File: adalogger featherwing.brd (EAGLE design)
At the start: 50.8 x 22.9 mm, 22 parts, among them IC1 RTC_PCF8523T, SW1 KMR2, X4 microsd, Y1 32khz

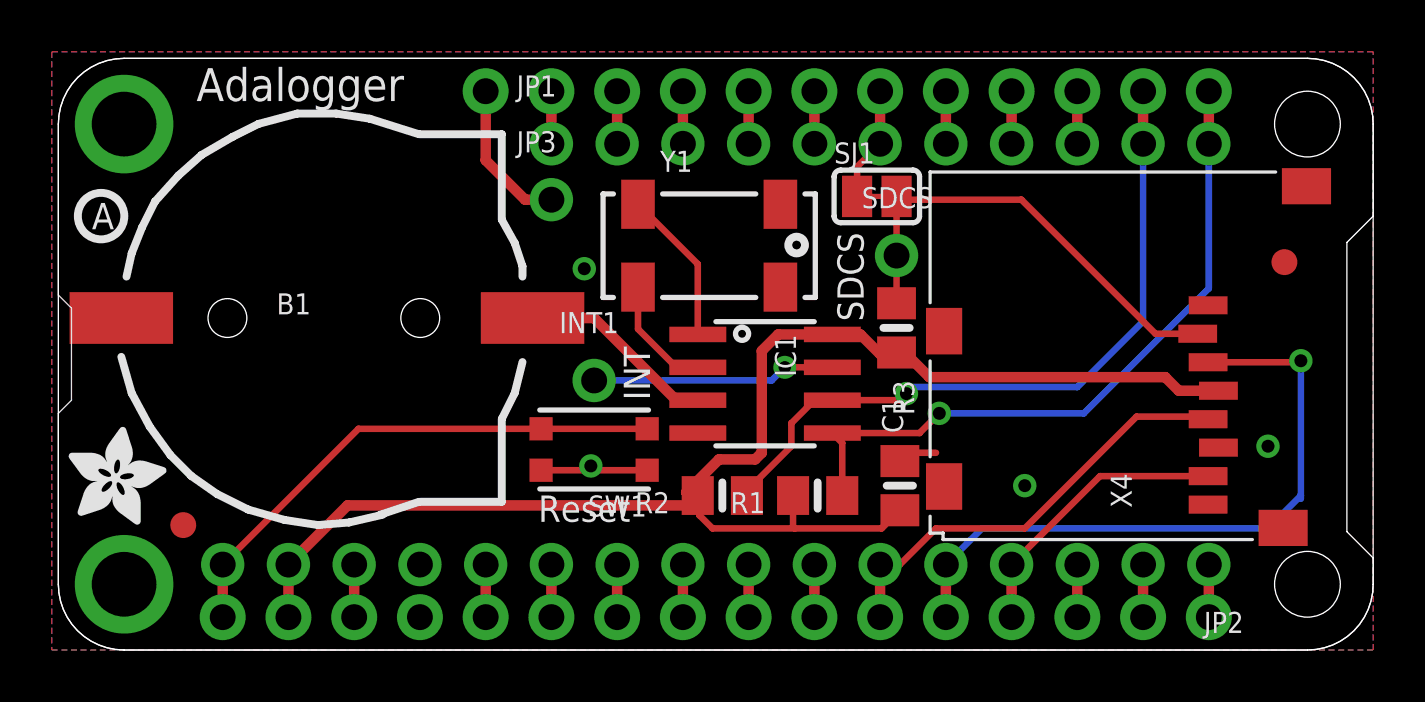
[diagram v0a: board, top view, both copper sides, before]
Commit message: update with RC filter
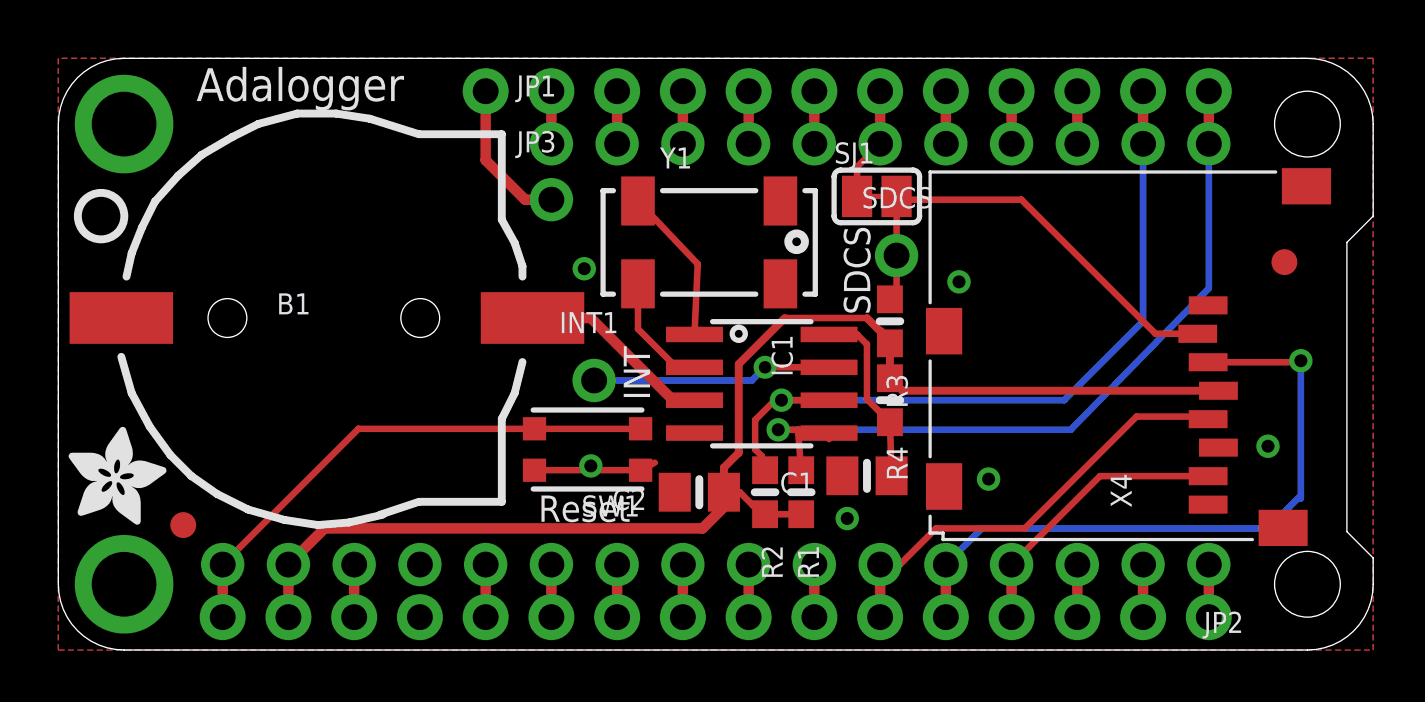
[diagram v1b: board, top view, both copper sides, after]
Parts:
- added C2: 10uF, microbuilder:0805-NO
- added R4: 1K, microbuilder:0603-NO
- FID1, FID2: value FIDUCIAL"" -> FIDUCIAL_1MM
- IC1: value RTC_PCF8523T -> PCF8523T
- MS1: device microbuilder:FEATHERWING_DIM -> microbuilder:FEATHERWING_NODIM
- R1, R2, R3: device microbuilder:0805-NO -> microbuilder:0603-NO
- moved R2 1.66 mm to (27.3, 6.10), turned to 270 degrees
- moved C1 1.33 mm to (31.2, 6.73), turned to 180 degrees
- moved R1 0.65 mm to (28.7, 6.10), turned to 270 degrees
- moved R3 0.36 mm to (32.1, 12.7)
- moved SW1 0.25 mm to (20.4, 7.75)
- moved IC1 0.13 mm to (27.2, 10.3)
- moved Y1 0.13 mm to (25.1, 15.7)
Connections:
- net D10 renamed CS
- net N$1 renamed RESET
- net N$10 renamed F
- net N$11 renamed E
- net N$12 renamed D
- net N$13 renamed C
- net N$14 renamed B
- net N$15 renamed A
- net N$16 renamed EN
- net N$17 renamed AREF
- net N$19 renamed L
- net N$2 renamed G
- net N$21 renamed J
- net N$22 renamed I
- net N$23 renamed H
- net N$3 renamed N
- net N$4 renamed TX
- net N$5 renamed M
- net N$6 renamed RX
- new net N$1: C1.1, IC1.8, R4.2
- net +3V3: now also C2.1, R4.1; no longer C1.1, IC1.8
- net GND: now also C2.2
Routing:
- net N$1: track 0.00 -> 7.07 mm
- net +3V3: track 56.4 -> 50.1 mm
- net SDA: track 29.1 -> 32.5 mm
- net SCL: track 29.6 -> 31.4 mm
- net GND: track 5.63 -> 4.72 mm, vias 4 -> 6
